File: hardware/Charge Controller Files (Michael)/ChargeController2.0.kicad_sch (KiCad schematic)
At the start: 82 parts, among them J1 Conn_01x02_Pin, J10 Conn-1x2, J11 Conn-1x2, J12 Conn-1x2, J13 Conn-1x2, J14 Conn-1x2, J15 Conn-1x2, J16 Conn-1x2, J17 SCL_MAS_01x01_Pin, J18 SDA_MAS_01x01_Pin, J2 SP_01x02_Pin, J3 SYS-1x2, J4 3.3V_PULLUP_01x01_Pin, J5 BATT_01x02_Pin, J6 Conn-1x2, J7 Conn-1x2, J8 Conn-1x2, J9 Conn-1x2, Q5 AONS66614, Q6 AONS66614, Q7 AONS66614, Q8 AONS66614, U1 BQ25756RRVR

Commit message: Inhibits Draft
Inhibits First Draft - MP
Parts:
- removed J1: Conn_01x02_Pin, symbol Connector:Conn_01x02_Pin
- removed J3: SYS-1x2, Connector_PinSocket_2.54mm:PinSocket_1x02_P2.54mm_Vertical, symbol Connector:Conn_01x02_Pin
- added D6, D7, D8, D9: D, symbol Device:D
- added J19: SYS-1x2, Connector_PinSocket_2.54mm:PinSocket_1x02_P2.54mm_Vertical, symbol Connector:Conn_01x02_Pin
- added Q1, Q10, Q11, Q12, Q2, Q3, Q4, Q9: NMOS, symbol Simulation_SPICE:NMOS
- added SW1: SW_DIP_x01, symbol Switch:SW_DIP_x01
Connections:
- net GND: now also C17.1, C18.1, R10.1, R13.1, R14.1, J19.2 (Pin_2), Q10.1 (D), Q12.3 (S), Q3.3 (S), Q9.1 (D); no longer J5.2 (Pin_2), U1.17 (PGND), U1.22 (PGND)
- net +36V: no longer names the net of C13.1, C2.1, C23.1, C4.1, C7.2, R11.1, R27.2, R3.1, R4.1, U1.32 (VAC), U1.33 (VAC)
- net +36V: now also Q2.3 (S); no longer J2.1 (Pin_1)
- new net: J19.1 (Pin_1), Q11.1 (D)
- new net: Q4.3 (S), Q9.3 (S)
- new net: Q1.3 (S), Q2.1 (D)
- new net: D7.1 (K), D8.1 (K), SW1.1
- new net: D8.2 (A), D9.1 (K)
- new net: D9.2 (A), J5.1 (Pin_1), Q3.1 (D)
- new net: J5.2 (Pin_2), Q4.1 (D)
- new net: D6.1 (K), D7.2 (A), Q1.1 (D)
- new net: Q10.3 (S), Q11.3 (S)
- new net: Q12.1 (D), U1.17 (PGND), U1.22 (PGND)
- new net: D6.2 (A), J2.1 (Pin_1)
- new net EN: Q1.2 (G), Q10.2 (G), Q11.2 (G), Q12.2 (G), Q2.2 (G), Q3.2 (G), Q4.2 (G), Q9.2 (G), SW1.2
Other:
- moved on the sheet: H1, H2, H3, H4, J2, J5

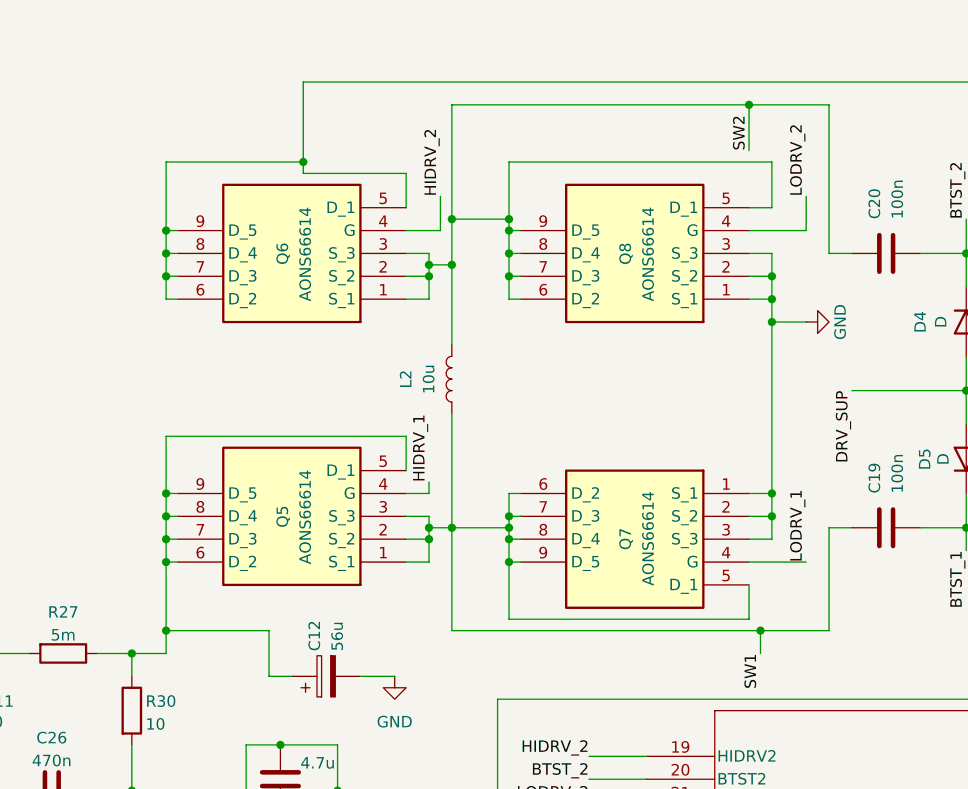
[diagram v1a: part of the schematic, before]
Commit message: Update MOSFET symbols
Update MOSFET symbols
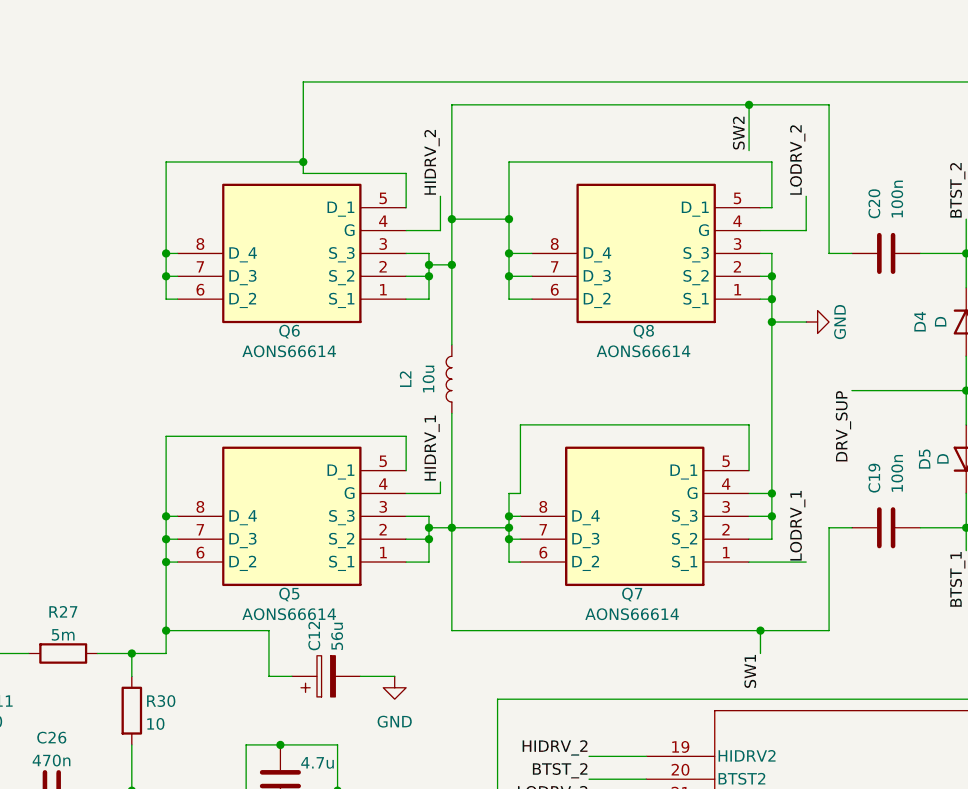
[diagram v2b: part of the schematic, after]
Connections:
- net GND: now also Q7.4 (G); no longer Q7.1 (S_1)
- net LODRV_1: now also Q7.1 (S_1); no longer Q7.4 (G)
- net SW1: no longer Q7.9 (D_5)
- net SW2: no longer Q8.9 (D_5)
- net at C24.1, Q6.5 (D_1), Q6.6 (D_2)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: no longer Q6.9 (D_5)
- net at C12.1, Q5.5 (D_1), Q5.6 (D_2)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: no longer Q5.9 (D_5)

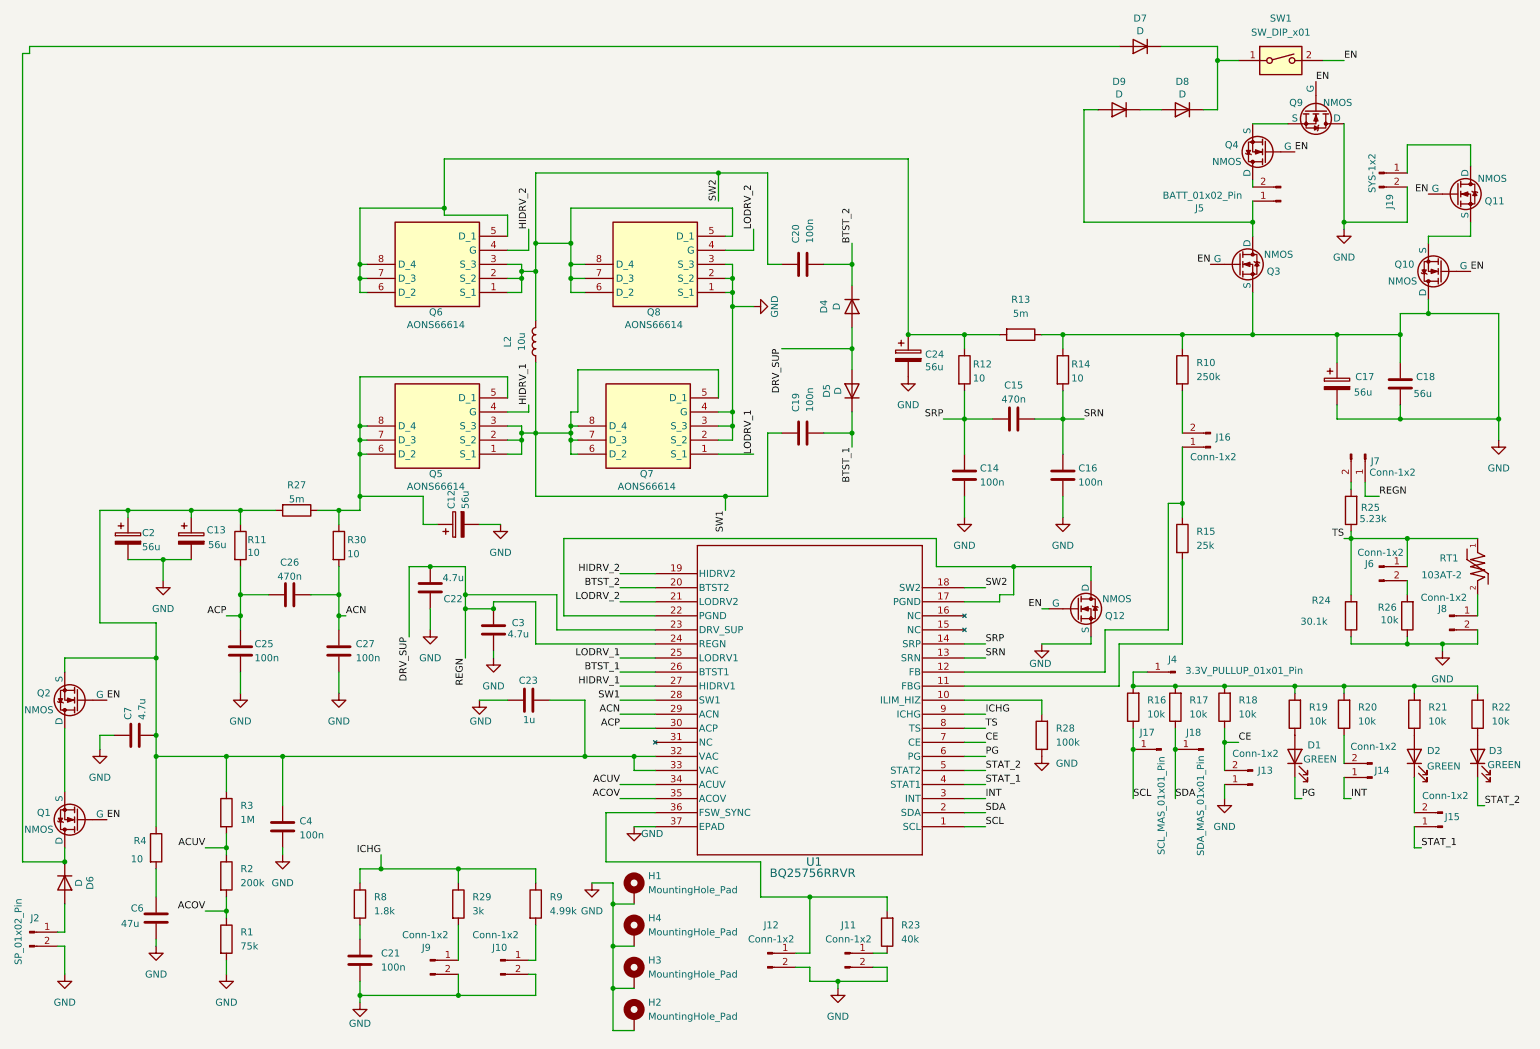
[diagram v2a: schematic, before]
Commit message: Updates
Added FPs, fixed ILIM_HIZ and ICHG vals, updated Inhibits system
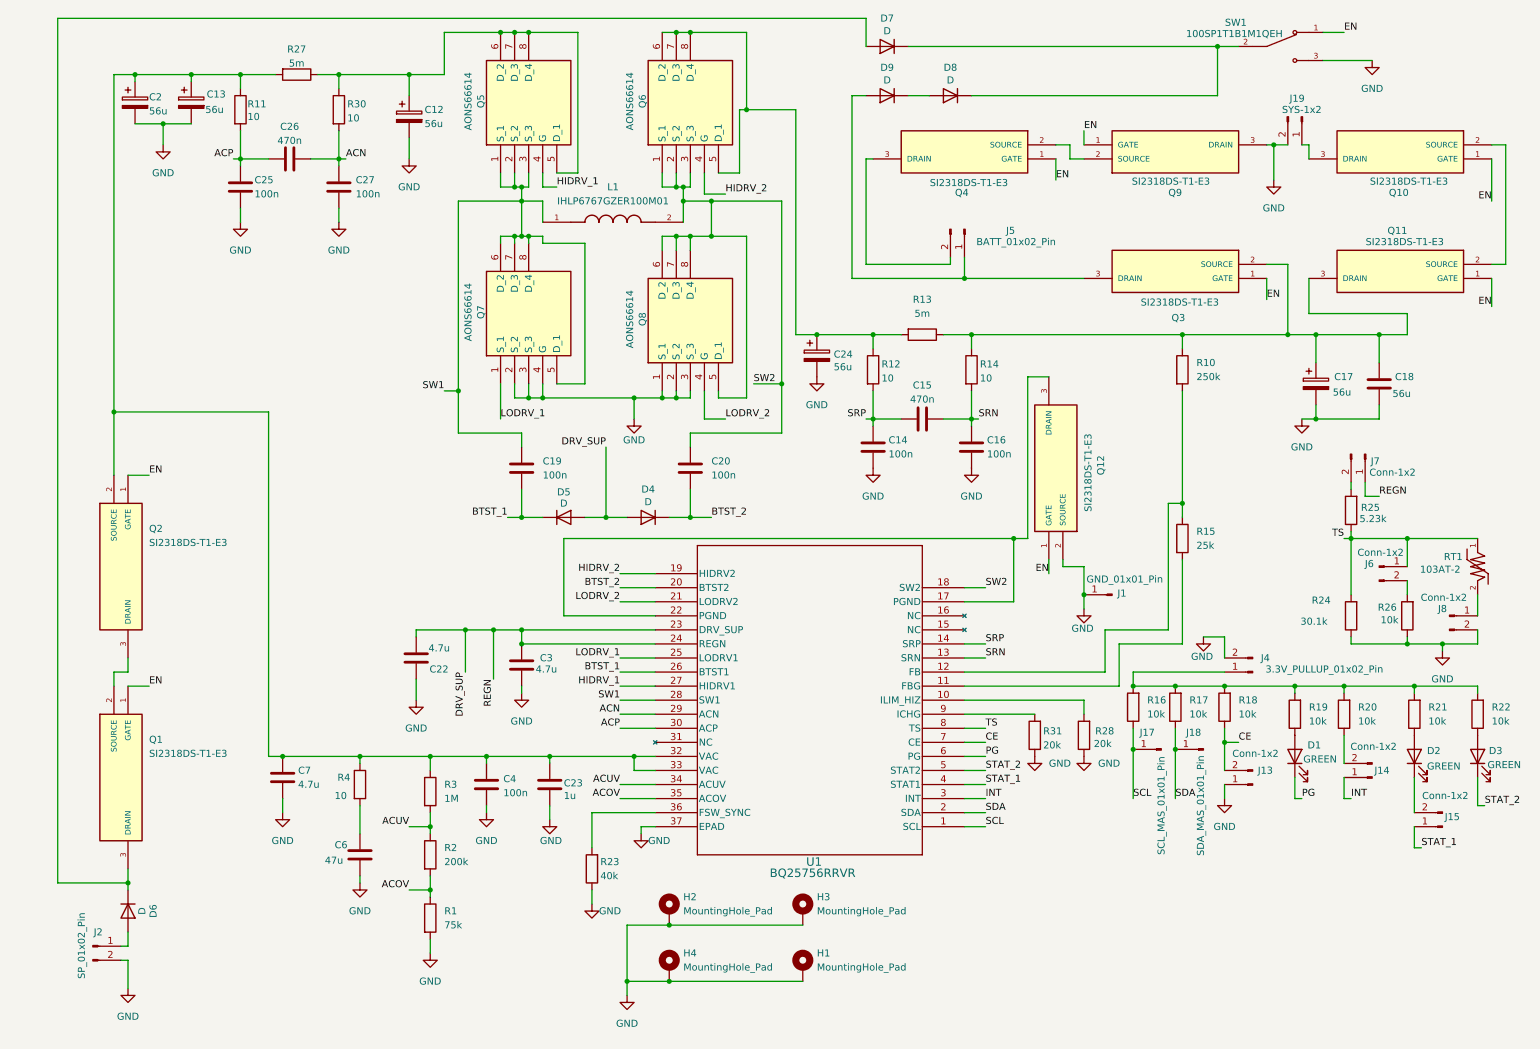
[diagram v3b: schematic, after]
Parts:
- removed C21: 100n, symbol Device:C
- removed J10, J11, J12, J16, J9: Conn-1x2, Connector_PinSocket_2.54mm:PinSocket_1x02_P2.54mm_Vertical, symbol Connector:Conn_01x02_Pin
- removed J4: 3.3V_PULLUP_01x01_Pin, symbol Connector:Conn_01x01_Pin
- removed L2: 10u, symbol Device:L
- removed Q1, Q10, Q11, Q12, Q2, Q3, Q4, Q9: NMOS, symbol Simulation_SPICE:NMOS
- removed R29: 3k, symbol Device:R
- removed R8: 1.8k, symbol Device:R
- removed R9: 4.99k, symbol Device:R
- removed SW1: SW_DIP_x01, symbol Switch:SW_DIP_x01
- added J1: GND_01x01_Pin, symbol Connector:Conn_01x01_Pin
- added J4: 3.3V_PULLUP_01x02_Pin, Connector_PinSocket_2.54mm:PinSocket_1x02_P2.54mm_Vertical, symbol Connector:Conn_01x02_Pin
- added L1: IHLP6767GZER100M01, IHLP6767GZER100M01:IND_IHLP6767GZER100M01, symbol IHLP6767GZER100M01:IHLP6767GZER100M01
- added Q10, Q11, Q12, Q2, Q3, Q4, Q9: SI2318DS-T1-E3, SI2318DS-T1-E3:SOT95P237X102-3N, symbol SI2318DS-T1-E3:SI2318DS-T1-E3
- added R31: 20k, symbol Device:R
- added SW1: 100SP1T1B1M1QEH, 100SP1T1B1M1QEH:SW_100SP1T1B1M1QEH, symbol 100SP1T1B1M1QEH:100SP1T1B1M1QEH
- R28: value 100k -> 20k
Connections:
- net EN: now also Q10.1 (GATE), Q11.1 (GATE), Q12.1 (GATE), Q2.1 (GATE), Q3.1 (GATE), Q4.1 (GATE), Q9.1 (GATE), SW1.1
- net GND: now also C7.2, R23.1, J1.1 (Pin_1), J4.2 (Pin_2), Q12.2 (SOURCE), Q9.3 (DRAIN), R31.1, SW1.3; no longer C17.1, C18.1, C7.1, R10.1, R13.1, R14.1
- net SW1: now also L1.1
- net SW2: now also L1.2
- net at J19.1 (Pin_1): now also Q10.3 (DRAIN)
- net at C13.1, C2.1, C23.1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: now also C7.1, Q2.2 (SOURCE); no longer C7.2
- net at D7.1 (K), D8.1 (K): now also SW1.2
- net at D9.2 (A), J5.1 (Pin_1): now also Q3.3 (DRAIN)
- net at J5.2 (Pin_2): now also Q4.3 (DRAIN)
- net at R16.2, R17.2, R18.2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: now also J4.1 (Pin_1)
- net at D6.1 (K), D7.2 (A): now also Q3.3 (DRAIN)
- net at R15.1, U1.12 (FB): now also R10.2
- net at U1.17 (PGND), U1.22 (PGND): now also Q12.3 (DRAIN)
- net ICHG: no longer names the net of U1.9 (ICHG)
- net ICHG: now also R31.2
- new net: Q10.2 (SOURCE), Q11.2 (SOURCE)
- new net: Q4.2 (SOURCE), Q9.2 (SOURCE)
- new net: C17.1, C18.1, Q11.3 (DRAIN), Q3.2 (SOURCE), R10.1, R13.1, R14.1
- new net: Q2.3 (DRAIN), Q3.2 (SOURCE)
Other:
- moved on the sheet: C12, C13, C14, C15, C16, C17, C18, C19, C2, C20, C22, C23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

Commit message: R/C name
R/C names
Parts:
- added J3: BATT_TEST_01x01_Pin, symbol Connector:Conn_01x01_Pin
- added J9: SYS_TEST_01x01_Pin, symbol Connector:Conn_01x01_Pin
- added Q3: SI2318DS-T1-E3, bmsfootprints:SOT95P237X102-3N, symbol SI2318DS-T1-E3:SI2318DS-T1-E3
- J1: value GND_01x01_Pin -> GND_TEST_01x01_Pin
- L1: footprint IHLP6767GZER100M01:IND_IHLP6767GZER100M01 -> bmsfootprints:IND_IHLP6767GZER100M01
- Q1: renamed from Q3; footprint SI2318DS-T1-E3:SOT95P237X102-3N -> bmsfootprints:SOT95P237X102-3N
- Q10, Q11, Q12, Q2, Q4, Q9: footprint SI2318DS-T1-E3:SOT95P237X102-3N -> bmsfootprints:SOT95P237X102-3N
- Q5, Q6, Q7, Q8: footprint AON6482 -> bmsfootprints:AON6482
- R1: value 75k -> 53.25
- R10: value 250k -> 249k
- R15: value 25k -> 16.67k
- R2: value 200k -> 11.83k
- R28: value 20k -> 16.67k
- R31: value 20k -> 25k
- RT1: footprint 103AT-2:103AT-2 -> bmsfootprints:103AT-2
- SW1: footprint 100SP1T1B1M1QEH:SW_100SP1T1B1M1QEH -> bmsfootprints:SW_100SP1T1B1M1QEH
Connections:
- net EN: now also Q3.1 (GATE)
- net at J19.1 (Pin_1), Q10.3 (DRAIN): now also J9.1 (Pin_1)
- net at D9.2 (A), J5.1 (Pin_1): now also J3.1 (Pin_1), Q3.3 (DRAIN); no longer Q1.3 (DRAIN)
- net at C17.1, C18.1, Q11.3 (DRAIN)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: now also Q3.2 (SOURCE); no longer Q1.2 (SOURCE)
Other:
- moved on the sheet: D6, Q10

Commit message: Change try II
Change try II
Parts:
- renumbered R13 to RR_BATT_SNS, R3 to R_AC1, R2 to R_AC2, R1 to R_AC3, R27 to R_AC_SNS, R10 to R_FB, R15 to R_FBG, R23 to R_FSW_SYNC, R28 to R_ICHG, R31 to R_ILIM_HIZ
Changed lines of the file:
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@@
 		(dnp no)
 		(fields_autoplaced yes)
-		(property "Reference" "R1"
+		(property "Reference" "R_AC3"
 			(at 90.17 175.2599 0)
 			(effects
@@
 			(project ""
 				(path "/89a953c5-1b9f-4ec7-83f7-649f6dcfa61f"
-					(reference "R1")
+					(reference "R_AC3")
 					(unit 1)
 				)
@@
 		(dnp no)
 		(fields_autoplaced yes)
-		(property "Reference" "R3"
+		(property "Reference" "R_AC1"
 			(at 90.17 152.3999 0)
 			(effects
@@
 			(project "ChargeController2.0"
 				(path "/89a953c5-1b9f-4ec7-83f7-649f6dcfa61f"
-					(reference "R3")
+					(reference "R_AC1")
 					(unit 1)
 				)
@@
 		(on_board yes)
 		(dnp no)
-		(property "Reference" "R27"
+		(property "Reference" "R_AC_SNS"
 			(at 63.5 19.558 90)
 			(effects
@@
 			(project "ChargeController2.0"
 				(path "/89a953c5-1b9f-4ec7-83f7-649f6dcfa61f"
-					(reference "R27")
+					(reference "R_AC_SNS")
 					(unit 1)
 				)
@@
 		(on_board yes)
 		(dnp no)
-		(property "Reference" "R31"
-			(at 198.374 142.748 0)
+		(property "Reference" "R_ILIM_HIZ"
+			(at 194.31 139.192 0)
 			(effects
 				(font
@@
 			(project "ChargeController2.0"
 				(path "/89a953c5-1b9f-4ec7-83f7-649f6dcfa61f"
-					(reference "R31")
+					(reference "R_ILIM_HIZ")
 					(unit 1)
 				)
@@
 		(on_board yes)
 		(dnp no)
-		(property "Reference" "R28"
-			(at 207.772 142.748 0)
+		(property "Reference" "R_ICHG"
+			(at 207.01 142.494 0)
 			(effects
 				(font
@@
 			(project ""
 				(path "/89a953c5-1b9f-4ec7-83f7-649f6dcfa61f"
-					(reference "R28")
+					(reference "R_ICHG")
 					(unit 1)
 				)
@@
 		(dnp no)
 		(fields_autoplaced yes)
-		(property "Reference" "R2"
+		(property "Reference" "R_AC2"
 			(at 90.17 163.8299 0)
 			(effects
@@
 			(project "ChargeController2.0"
 				(path "/89a953c5-1b9f-4ec7-83f7-649f6dcfa61f"
-					(reference "R2")
+					(reference "R_AC2")
 					(unit 1)
 				)
@@
 		)
 		(property "Value" "GND_TEST_01x01_Pin"
-			(at 217.17 115.57 0)
+			(at 216.408 116.078 0)
 			(effects
 				(font
@@
 		(on_board yes)
 		(dnp no)
-		(property "Reference" "R23"
+		(property "Reference" "R_FSW_SYNC"
 			(at 118.364 166.37 0)
 			(effects
@@
 			(project "ChargeController2.0"
 				(path "/89a953c5-1b9f-4ec7-83f7-649f6dcfa61f"
-					(reference "R23")
+					(reference "R_FSW_SYNC")
 					(unit 1)
 				)
@@
 		(dnp no)
 		(fields_autoplaced yes)
-		(property "Reference" "R13"
+		(property "Reference" "RR_BATT_SNS"
 			(at 176.53 64.77 90)
 			(effects
@@
 			(project "ChargeController2.0"
 				(path "/89a953c5-1b9f-4ec7-83f7-649f6dcfa61f"
-					(reference "R13")
+					(reference "RR_BATT_SNS")
 					(unit 1)
 				)
@@
 		(dnp no)
 		(fields_autoplaced yes)
-		(property "Reference" "R10"
+		(property "Reference" "R_FB"
 			(at 226.06 76.1999 0)
 			(effects
@@
 			(project ""
 				(path "/89a953c5-1b9f-4ec7-83f7-649f6dcfa61f"
-					(reference "R10")
+					(reference "R_FB")
 					(unit 1)
 				)
@@
 		(dnp no)
 		(fields_autoplaced yes)
-		(property "Reference" "R15"
+		(property "Reference" "R_FBG"
 			(at 226.06 106.6799 0)
 			(effects
@@
 			(project ""
 				(path "/89a953c5-1b9f-4ec7-83f7-649f6dcfa61f"
-					(reference "R15")
+					(reference "R_FBG")
 					(unit 1)
 				)

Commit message: main
main
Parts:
- added J10: SOL_TEST_01x01_Pin, symbol Connector:Conn_01x01_Pin
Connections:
- net at D6.2 (A), J2.1 (Pin_1): now also J10.1 (Pin_1)
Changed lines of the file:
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@@
 	)
 	(junction
+		(at 38.1 181.61)
+		(diameter 0)
+		(color 0 0 0 0)
+	)
+	(junction
 		(at 83.82 24.13)
 		(diameter 0)
@@
 	(wire
 		(pts
+			(xy 38.1 181.61) (xy 40.64 181.61)
+		)
+		(stroke
+			(width 0)
+			(type default)
+		)
+	)
+	(wire
+		(pts
 			(xy 121.92 142.24) (xy 128.27 142.24)
 		)
@@
 					(unit 1)
 				)
+			)
+		)
+	)
+	(symbol
+		(lib_id "Connector:Conn_01x01_Pin")
+		(at 45.72 181.61 180)
+		(unit 1)
+		(exclude_from_sim no)
+		(in_bom yes)
+		(on_board yes)
+		(dnp no)
+		(property "Reference" "J10"
+			(at 48.006 181.864 0)
+			(effects
+				(font
+					(size 1.27 1.27)
+				)
+			)
+		)
+		(property "Value" "SOL_TEST_01x01_Pin"
+			(at 55.372 184.912 0)
+			(effects
+				(font
+					(size 1.27 1.27)
+				)
+			)
+		)
+		(property "Footprint" ""
+			(at 45.72 181.61 0)
+			(effects
+				(font
+					(size 1.27 1.27)
+				)
+				(hide yes)
+			)
+		)
+		(property "Datasheet" "~"
+			(at 45.72 181.61 0)
+			(effects
+				(font
+					(size 1.27 1.27)
+				)
+				(hide yes)
+			)
+		)
+		(property "Description" "Generic connector, single row, 01x01, script generated"
+			(at 45.72 181.61 0)
+			(effects
+				(font
+					(size 1.27 1.27)
+				)
+				(hide yes)
+			)
+		)
+		(pin "1"
+		)
+		(instances
+			(project "ChargeController2.0"
+				(path "/89a953c5-1b9f-4ec7-83f7-649f6dcfa61f"
+					(reference "J10")
+					(unit 1)
+				)
